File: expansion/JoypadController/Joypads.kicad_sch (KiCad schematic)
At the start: 23 parts, among them J3 Joystick 1, J4 Joystick 2, U3 74LS574, U4 74LS574

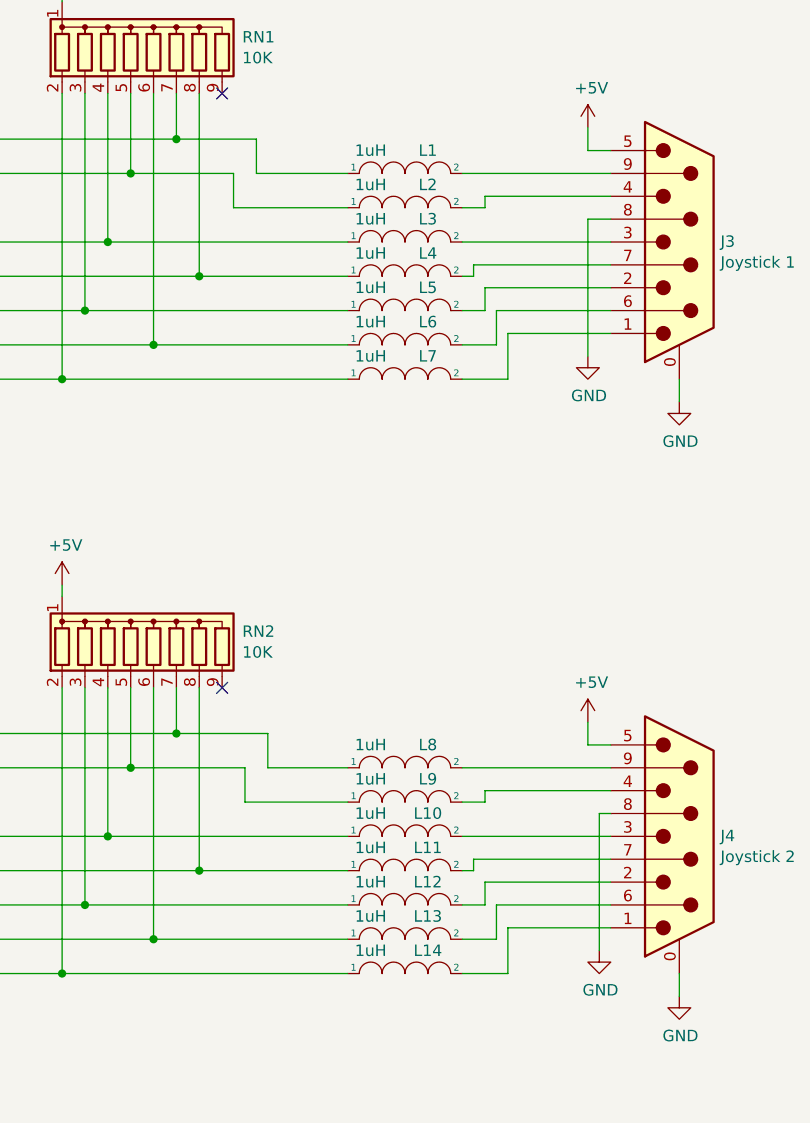
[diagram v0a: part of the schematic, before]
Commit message: All projects updated to KiCAD 7 format files
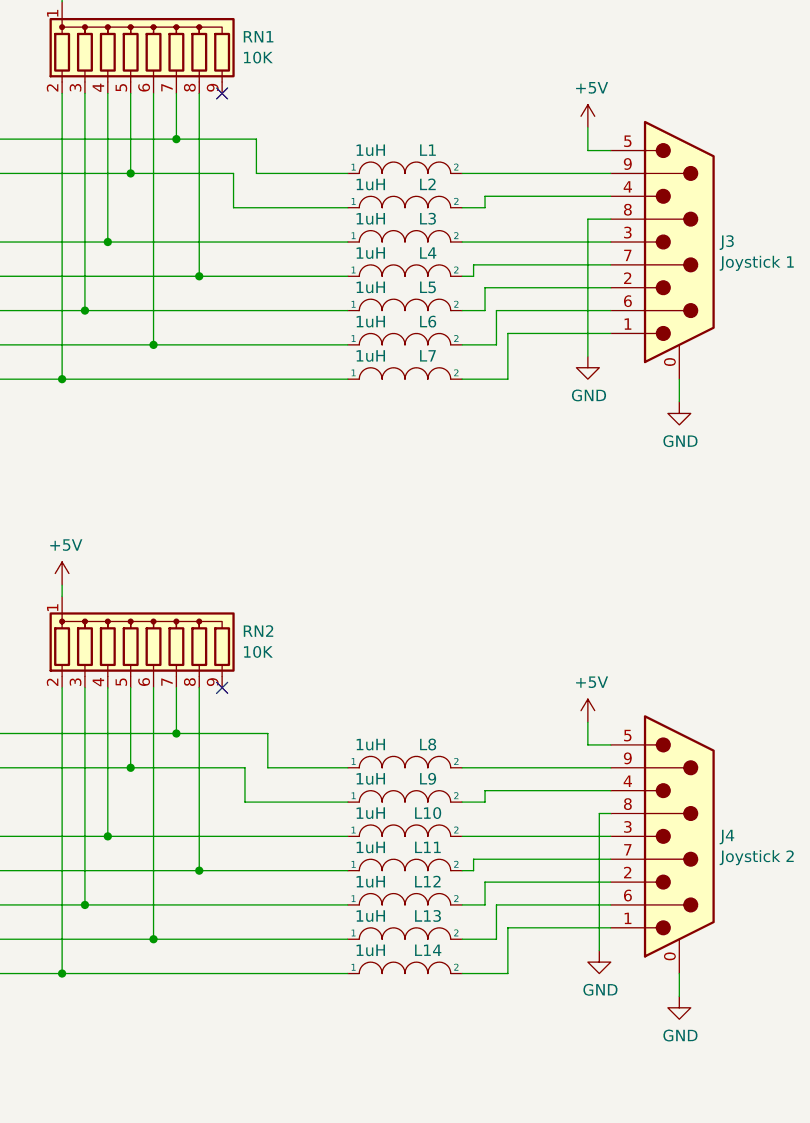
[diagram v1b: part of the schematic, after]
